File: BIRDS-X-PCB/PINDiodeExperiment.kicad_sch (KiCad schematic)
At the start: 84 parts, among them Q1 MMBF4392LT1G, U1 LM358DR

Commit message: Update footprint assignments
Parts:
- C1, C2, C3, C4, C5: footprint Capacitors_SMD:C_0603_HandSoldering -> Capacitor_SMD:C_0805_2012Metric_Pad1.18x1.45mm_HandSolder
- C6, C7: footprint Capacitors_SMD:CP_Elec_6.3x5.8 -> Capacitor_SMD:CP_Elec_6.3x5.8
- D1: footprint Diodes_ThroughHole:D_DO-201_P5.08mm_Vertical_AnodeUp -> OptoDevice:Osram_DIL2_4.3x4.65mm_P5.08mm
- JP601: renamed from JP1; footprint (none) -> Jumper:SolderJumper-2_P1.3mm_Open_RoundedPad1.0x1.5mm
- JP602: renamed from JP3; footprint (none) -> Jumper:SolderJumper-2_P1.3mm_Open_RoundedPad1.0x1.5mm
- JP603: renamed from JP2; footprint (none) -> Jumper:SolderJumper-2_P1.3mm_Open_RoundedPad1.0x1.5mm
- JP604: renamed from JP4; footprint (none) -> Jumper:SolderJumper-2_P1.3mm_Open_RoundedPad1.0x1.5mm
- Q1: footprint TO_SOT_Packages_SMD:SOT-23 -> Package_TO_SOT_SMD:SOT-23
- R1, R10, R2, R3, R4, R5, R6, R7, R8, R9: footprint Resistors_SMD:R_0603_HandSoldering -> Resistor_SMD:R_0805_2012Metric_Pad1.20x1.40mm_HandSolder
- U1: footprint Housings_SOIC:SOIC-8_3.9x4.9mm_Pitch1.27mm -> Package_SO:SOIC-8_3.9x4.9mm_P1.27mm

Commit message: Update footprints to 0603
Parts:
- C1, C2, C3, C4, C5: footprint Capacitor_SMD:C_0805_2012Metric_Pad1.18x1.45mm_HandSolder -> Capacitor_SMD:C_0603_1608Metric_Pad1.08x0.95mm_HandSolder
- C6, C7: footprint Capacitor_SMD:CP_Elec_6.3x5.8 -> Capacitor_SMD:C_1206_3216Metric_Pad1.33x1.80mm_HandSolder
- R1, R10, R2, R3, R4, R5, R6, R7, R8, R9: footprint Resistor_SMD:R_0805_2012Metric_Pad1.20x1.40mm_HandSolder -> Resistor_SMD:R_0603_1608Metric_Pad0.98x0.95mm_HandSolder

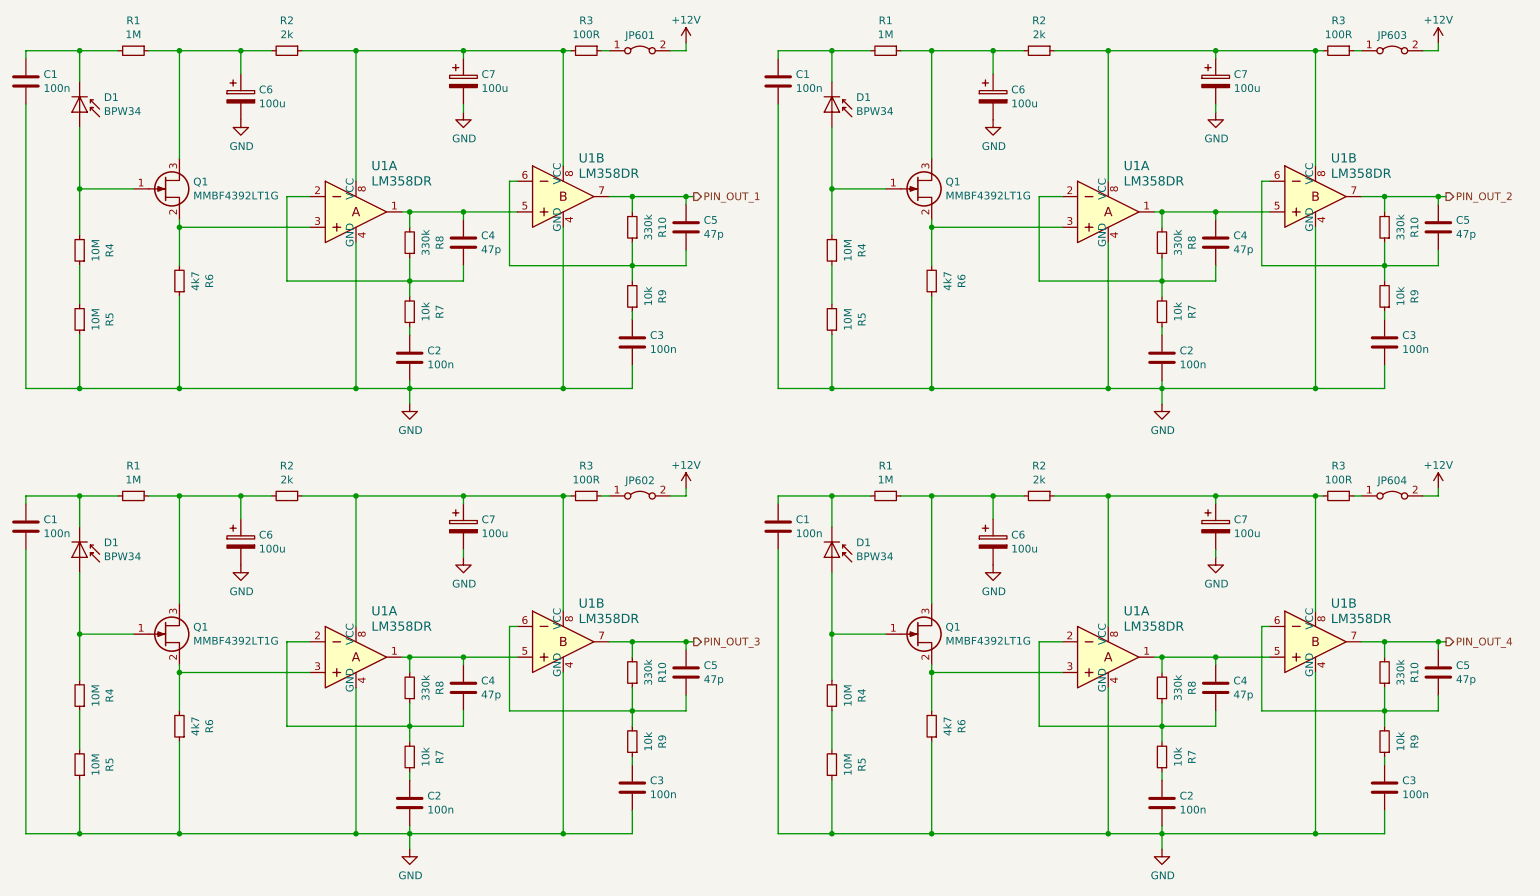
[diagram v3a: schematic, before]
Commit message: Re-organize PIN diode sheet structure
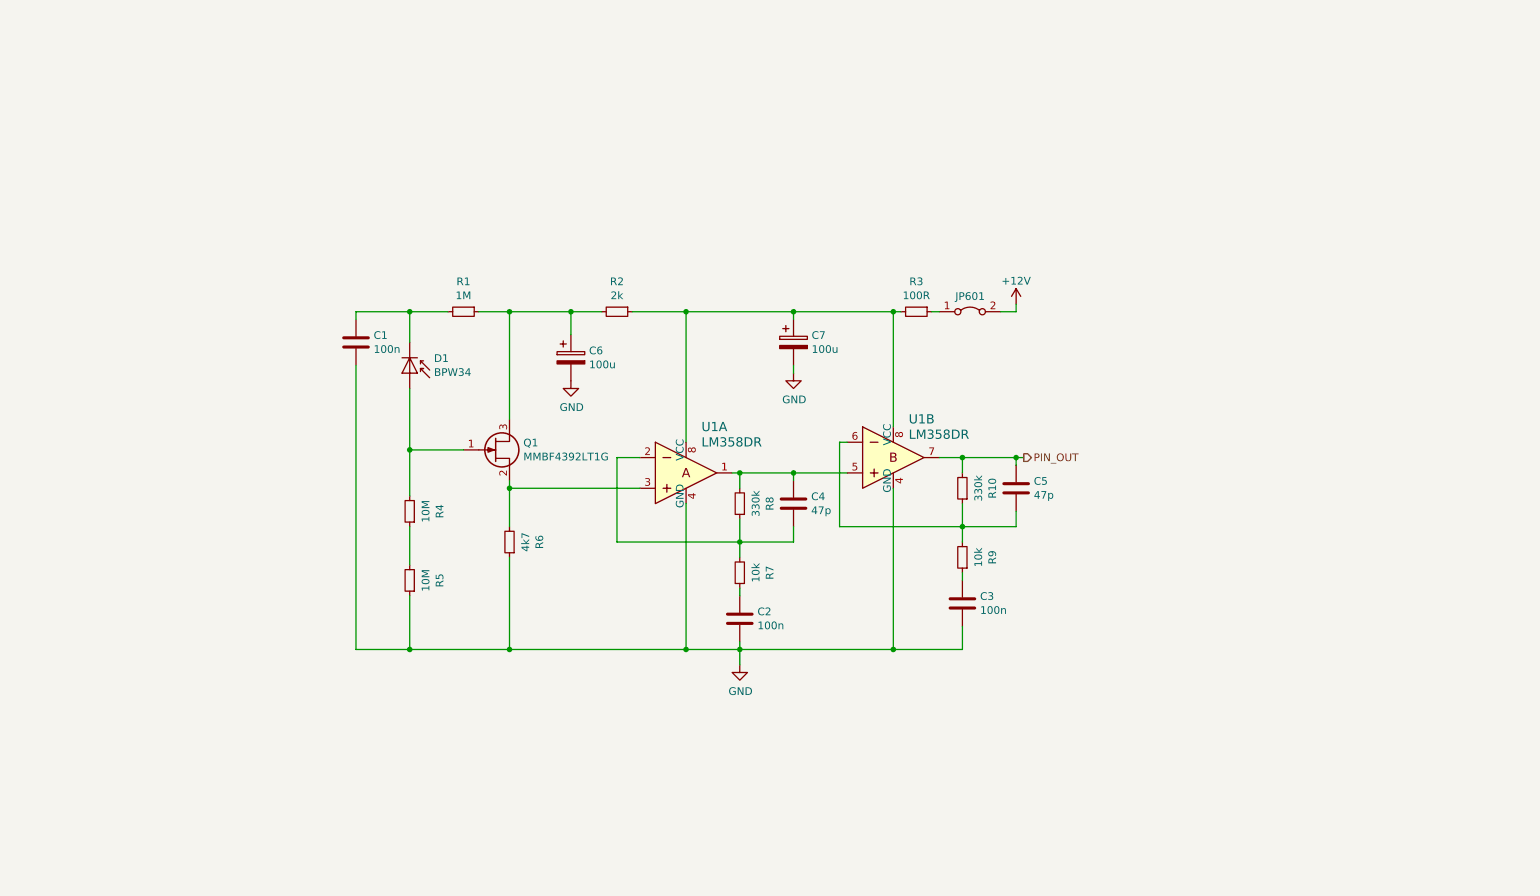
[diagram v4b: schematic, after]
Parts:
- removed C1 (x3), C2 (x3), C3 (x3): 100n, Capacitor_SMD:C_0603_1608Metric_Pad1.08x0.95mm_HandSolder, symbol Device:C
- removed C4 (x3), C5 (x3): 47p, Capacitor_SMD:C_0603_1608Metric_Pad1.08x0.95mm_HandSolder, symbol Device:C
- removed C6 (x3), C7 (x3): 100u, Capacitor_SMD:C_1206_3216Metric_Pad1.33x1.80mm_HandSolder, symbol PIN_Radiation_Detector-rescue:CP-Device
- removed D1 (x3): BPW34, OptoDevice:Osram_DIL2_4.3x4.65mm_P5.08mm, symbol Sensor_Optical:BPW34
- removed JP602, JP603, JP604: Jumper_2_Bridged, Jumper:SolderJumper-2_P1.3mm_Open_RoundedPad1.0x1.5mm, symbol Jumper:Jumper_2_Bridged
- removed Q1 (x3): MMBF4392LT1G, Package_TO_SOT_SMD:SOT-23, symbol Transistor_FET:BF245B
- removed R1 (x3): 1M, Resistor_SMD:R_0603_1608Metric_Pad0.98x0.95mm_HandSolder, symbol Device:R_Small
- removed R10 (x3), R8 (x3): 330k, Resistor_SMD:R_0603_1608Metric_Pad0.98x0.95mm_HandSolder, symbol Device:R_Small
- removed R2 (x3): 2k, Resistor_SMD:R_0603_1608Metric_Pad0.98x0.95mm_HandSolder, symbol Device:R_Small
- removed R3 (x3): 100R, Resistor_SMD:R_0603_1608Metric_Pad0.98x0.95mm_HandSolder, symbol Device:R_Small
- removed R4 (x3), R5 (x3): 10M, Resistor_SMD:R_0603_1608Metric_Pad0.98x0.95mm_HandSolder, symbol Device:R_Small
- removed R6 (x3): 4k7, Resistor_SMD:R_0603_1608Metric_Pad0.98x0.95mm_HandSolder, symbol Device:R_Small
- removed R7 (x3), R9 (x3): 10k, Resistor_SMD:R_0603_1608Metric_Pad0.98x0.95mm_HandSolder, symbol Device:R_Small
- removed U1 (x3): LM358DR, Package_SO:SOIC-8_3.9x4.9mm_P1.27mm, symbol PIN_Radiation_Detector-rescue:LM358DR-dk_Linear-Amplifiers-Instrumentation-OP-A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
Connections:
- net PIN_OUT_1 renamed PIN_OUT
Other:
- moved on the sheet: C1, C2, C3, C4, C5, C6, C7, D1, JP601, Q1, R1, R10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

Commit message: Finish most routing
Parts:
- C6, C7: symbol PIN_Radiation_Detector-rescue:CP-Device -> Device:C_Polarized
- U1: symbol PIN_Radiation_Detector-rescue:LM358DR-dk_Linear-Amplifiers-Instrumentation-OP-Amps-Buffer-Amps -> BIRDS-X_Symbols_Lib:LM358DR-dk_Linear-Amplifiers-Instrumentation-OP-Amps-Buffer-Amps
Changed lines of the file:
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@@
     )
   )
-  (symbol (lib_id "PIN_Radiation_Detector-rescue:CP-Device") (at 109.22 71.12 0) (unit 1)
+  (symbol (lib_id "Device:C_Polarized") (at 109.22 71.12 0) (unit 1)
     (in_bom yes) (on_board yes) (dnp no)
     (property "Reference" "C6" (at 112.2172 69.9516 0)
@@
     )
   )
-  (symbol (lib_id "PIN_Radiation_Detector-rescue:LM358DR-dk_Linear-Amplifiers-Instrumentation-OP-Amps-Buffer-Amps") (at 162.56 87.63 0) (unit 2)
+  (symbol (lib_id "BIRDS-X_Symbols_Lib:LM358DR-dk_Linear-Amplifiers-Instrumentation-OP-Amps-Buffer-Amps") (at 162.56 87.63 0) (unit 2)
     (in_bom yes) (on_board yes) (dnp no)
     (property "Reference" "U1" (at 165.1 81.28 0)
@@
     )
   )
-  (symbol (lib_id "PIN_Radiation_Detector-rescue:LM358DR-dk_Linear-Amplifiers-Instrumentation-OP-Amps-Buffer-Amps") (at 128.27 90.17 0) (unit 1)
+  (symbol (lib_id "BIRDS-X_Symbols_Lib:LM358DR-dk_Linear-Amplifiers-Instrumentation-OP-Amps-Buffer-Amps") (at 128.27 90.17 0) (unit 1)
     (in_bom yes) (on_board yes) (dnp no)
     (property "Reference" "U1" (at 130.81 82.55 0)
@@
     )
   )
-  (symbol (lib_id "PIN_Radiation_Detector-rescue:CP-Device") (at 146.05 68.58 0) (unit 1)
+  (symbol (lib_id "Device:C_Polarized") (at 146.05 68.58 0) (unit 1)
     (in_bom yes) (on_board yes) (dnp no)
     (property "Reference" "C7" (at 149.0472 67.4116 0)
